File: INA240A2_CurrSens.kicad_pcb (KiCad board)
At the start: 2 copper layers, 31.4 x 28.2 mm, 17 parts, among them J1 Conn_01x01_Pin, J2 Conn_01x01_Pin, J3 Conn_01x01_Pin, J4 Conn_01x01_Pin, J5 Conn_01x01_Pin, J6 Conn_01x01_Pin, J7 Conn_01x01_Pin, J8 Conn_01x01_Pin, U1 INA240A2D, U2 INA240A2D

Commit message: Upload KiCad schematic and PCB layout
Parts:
- renumbered J7 to 3.3V, J5 to ADC_1, J6 to ADC_2, J1 to B_1, J3 to B_2, J2 to D_1, J4 to D_2, J8 to GND
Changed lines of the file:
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@@
 		(descr "Through hole straight socket strip, 1x01, 2.54mm pitch, single row (from Kicad 4.0.7), script generated")
 		(tags "Through hole socket strip THT 1x01 2.54mm single row")
-		(property "Reference" "J5"
+		(property "Reference" "ADC_1"
 			(at 0 -2.77 0)
 			(layer "F.SilkS")
@@
 		(descr "Through hole straight socket strip, 1x01, 2.54mm pitch, single row (from Kicad 4.0.7), script generated")
 		(tags "Through hole socket strip THT 1x01 2.54mm single row")
-		(property "Reference" "J6"
+		(property "Reference" "ADC_2"
 			(at 0 -2.77 0)
 			(layer "F.SilkS")
@@
 		(descr "Through hole straight socket strip, 1x01, 2.54mm pitch, single row (from Kicad 4.0.7), script generated")
 		(tags "Through hole socket strip THT 1x01 2.54mm single row")
-		(property "Reference" "J2"
+		(property "Reference" "D_1"
 			(at 0 -2.77 0)
 			(layer "F.SilkS")
@@
 		(descr "Through hole straight socket strip, 1x01, 2.54mm pitch, single row (from Kicad 4.0.7), script generated")
 		(tags "Through hole socket strip THT 1x01 2.54mm single row")
-		(property "Reference" "J1"
+		(property "Reference" "B_1"
 			(at 0 -2.77 0)
 			(layer "F.SilkS")
@@
 		(descr "Through hole straight socket strip, 1x01, 2.54mm pitch, single row (from Kicad 4.0.7), script generated")
 		(tags "Through hole socket strip THT 1x01 2.54mm single row")
-		(property "Reference" "J8"
+		(property "Reference" "GND"
 			(at 0 -2.77 0)
 			(layer "F.SilkS")
@@
 		(descr "Through hole straight socket strip, 1x01, 2.54mm pitch, single row (from Kicad 4.0.7), script generated")
 		(tags "Through hole socket strip THT 1x01 2.54mm single row")
-		(property "Reference" "J3"
+		(property "Reference" "B_2"
 			(at 0 -2.77 0)
 			(layer "F.SilkS")
@@
 		)
 		(fp_text user "${REFERENCE}"
-			(at 0 0 0)
+			(at 0 -1.947 0)
 			(layer "F.Fab")
 			(effects
@@
 		(descr "Through hole straight socket strip, 1x01, 2.54mm pitch, single row (from Kicad 4.0.7), script generated")
 		(tags "Through hole socket strip THT 1x01 2.54mm single row")
-		(property "Reference" "J7"
+		(property "Reference" "3.3V"
 			(at -0.29 -2.75 0)
 			(layer "F.SilkS")
@@
 		(descr "Through hole straight socket strip, 1x01, 2.54mm pitch, single row (from Kicad 4.0.7), script generated")
 		(tags "Through hole socket strip THT 1x01 2.54mm single row")
-		(property "Reference" "J4"
+		(property "Reference" "D_2"
 			(at 0 -2.77 0)
 			(layer "F.SilkS")

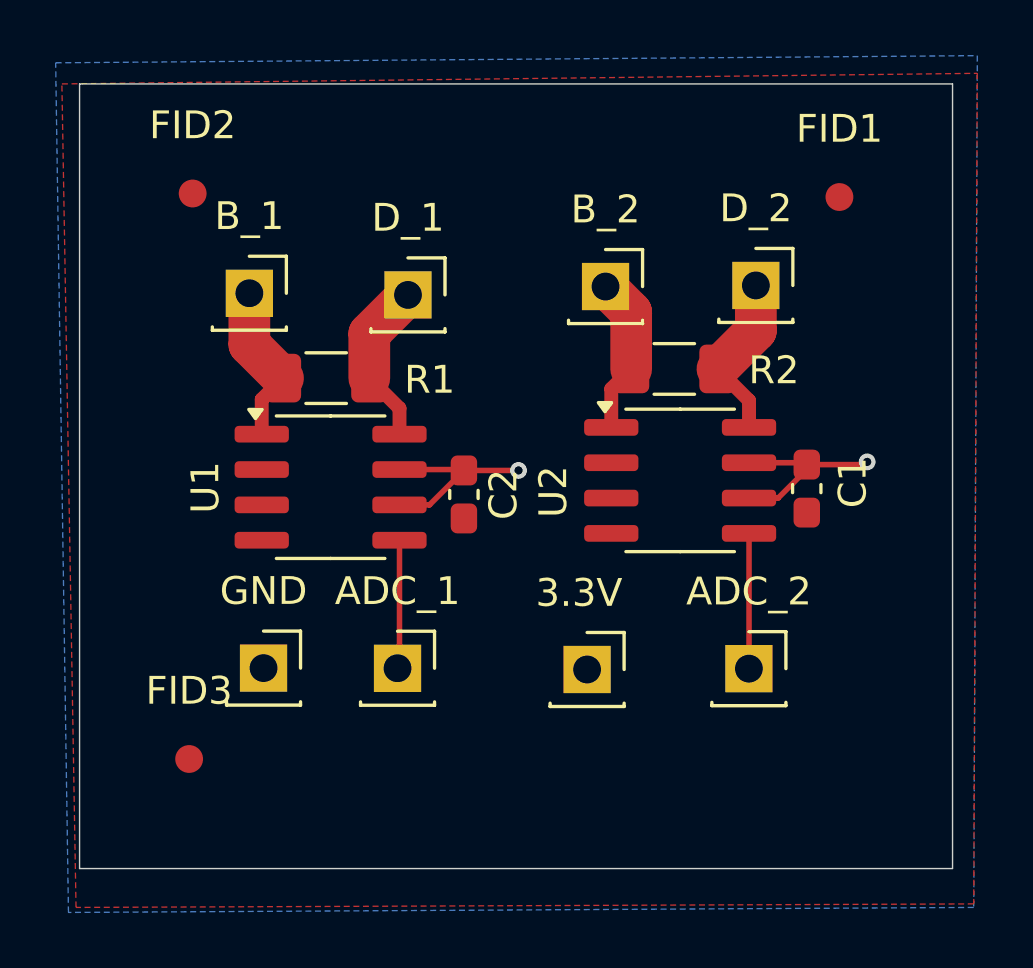
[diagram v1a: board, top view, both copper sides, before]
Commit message: added filled zones for voltage
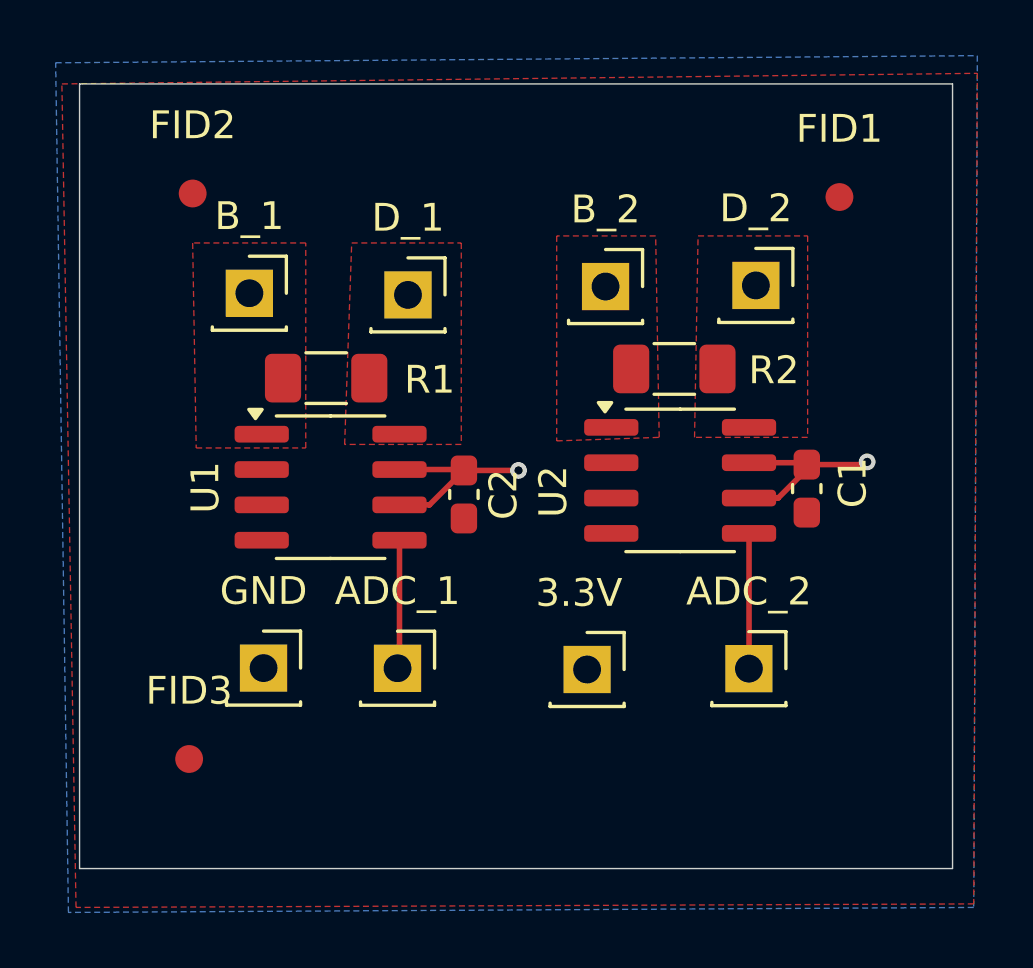
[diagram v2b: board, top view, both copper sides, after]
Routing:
- net /Driver_2: track 6.14 -> 0.00 mm
- net /Driver_1: track 6.03 -> 0.00 mm
- net /BLDC_1: track 5.88 -> 0.00 mm
- net /BLDC_2: track 5.74 -> 0.00 mm
- added copper zone on F.Cu, net /BLDC_1
- added copper zone on F.Cu, net /BLDC_2
- added copper zone on F.Cu, net /Driver_1
- added copper zone on F.Cu, net /Driver_2
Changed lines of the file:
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@@
-	)
-	(segment
-		(start 117.795 75.705)
-		(end 117.795 74.775)
-		(width 0.5)
-		(layer "F.Cu")
-		(net 3)
-	)
-	(segment
-		(start 116.71 73.69)
-		(end 116.71 72.09)
-		(width 1.5)
-		(layer "F.Cu")
-		(net 3)
-	)
-	(segment
-		(start 117.795 74.775)
-		(end 116.71 73.69)
-		(width 0.5)
-		(layer "F.Cu")
-		(net 3)
-	)
-	(segment
-		(start 116.71 72.09)
-		(end 118.1 70.7)
-		(width 1.5)
-		(layer "F.Cu")
-		(net 3)
-	)
-	(segment
-		(start 112.4 70.64)
-		(end 112.4 72.48)
-		(width 1.5)
-		(layer "F.Cu")
-		(net 4)
-	)
-	(segment
-		(start 112.845 74.455)
-		(end 113.61 73.69)
-		(width 0.5)
-		(layer "F.Cu")
-		(net 4)
-	)
-	(segment
-		(start 112.845 75.705)
-		(end 112.845 74.455)
-		(width 0.5)
-		(layer "F.Cu")
-		(net 4)
-	)
-	(segment
-		(start 112.4 72.48)
-		(end 113.61 73.69)
-		(width 1.5)
-		(layer "F.Cu")
-		(net 4)
-	)
-	(segment
-		(start 130.355 75.46)
-		(end 130.355 74.495)
-		(width 0.5)
-		(layer "F.Cu")
-		(net 5)
-	)
-	(segment
-		(start 130.6 70.36)
-		(end 130.6 71.98)
-		(width 1.5)
-		(layer "F.Cu")
-		(net 5)
-	)
-	(segment
-		(start 130.6 71.98)
-		(end 129.22 73.36)
-		(width 1.5)
-		(layer "F.Cu")
-		(net 5)
-	)
-	(segment
-		(start 130.355 74.495)
-		(end 129.22 73.36)
-		(width 0.5)
-		(layer "F.Cu")
-		(net 5)
-	)
-	(segment
-		(start 125.405 74.075)
-		(end 126.12 73.36)
-		(width 0.5)
-		(layer "F.Cu")
-		(net 6)
-	)
-	(segment
-		(start 126.12 73.36)
-		(end 126.12 71.32)
-		(width 1.5)
-		(layer "F.Cu")
-		(net 6)
-	)
-	(segment
-		(start 126.12 71.32)
-		(end 125.2 70.4)
-		(width 1.5)
-		(layer "F.Cu")
-		(net 6)
-	)
-	(segment
-		(start 125.405 75.46)
-		(end 125.405 74.075)
-		(width 0.5)
-		(layer "F.Cu")
-		(net 6)
 	)
 	(segment
@@
 	)
 	(zone
+		(net 6)
+		(net_name "/BLDC_2")
+		(layer "F.Cu")
+		(hatch edge 0.5)
+		(priority 4)
+		(connect_pads
+			(clearance 0.5)
+		)
+		(min_thickness 0.25)
+		(filled_areas_thickness no)
+		(fill yes
+			(thermal_gap 0.5)
+			(thermal_bridge_width 0.5)
+		)
+		(polygon
+			(pts
+				(xy 123.444 68.58) (xy 123.444 75.946) (xy 127.127 75.819) (xy 127 68.58)
+			)
+		)
+	)
+	(zone
+		(net 5)
+		(net_name "/Driver_2")
+		(layer "F.Cu")
+		(hatch edge 0.5)
+		(priority 5)
+		(connect_pads
+			(clearance 0.5)
+		)
+		(min_thickness 0.25)
+		(filled_areas_thickness no)
+		(fill yes
+			(thermal_gap 0.5)
+			(thermal_bridge_width 0.5)
+		)
+		(polygon
+			(pts
+				(xy 128.397 75.819) (xy 128.524 68.58) (xy 132.461 68.58) (xy 132.461 75.819)
+			)
+		)
+	)
+	(zone
+		(net 4)
+		(net_name "/BLDC_1")
+		(layer "F.Cu")
+		(hatch edge 0.5)
+		(priority 2)
+		(connect_pads
+			(clearance 0.5)
+		)
+		(min_thickness 0.25)
+		(filled_areas_thickness no)
+		(fill yes
+			(thermal_gap 0.5)
+			(thermal_bridge_width 0.5)
+		)
+		(polygon
+			(pts
+				(xy 114.427 76.2) (xy 114.427 68.834) (xy 110.363 68.834) (xy 110.49 76.2)
+			)
+		)
+	)
+	(zone
 		(net 2)
 		(net_name "GND")
@@
 			)
 		)
+	)
+	(zone
+		(net 3)
+		(net_name "/Driver_1")
+		(layer "F.Cu")
+		(hatch edge 0.5)
+		(priority 3)
+		(connect_pads
+			(clearance 0.5)
+		)
+		(min_thickness 0.25)
+		(filled_areas_thickness no)
+		(fill yes
+			(thermal_gap 0.5)
+			(thermal_bridge_width 0.5)
+		)
+		(polygon
+			(pts
+				(xy 116.078 68.834) (xy 120.015 68.834) (xy 120.015 76.073) (xy 115.824 76.073)
+			)
+		)
